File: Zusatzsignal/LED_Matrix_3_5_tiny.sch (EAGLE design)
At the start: 18 parts, among them IC3 ATTINY44SSU, Q1 IRLML5203, Q2 IRLML5203, Q3 IRLML5203, Q4 IRLML5203, Q5 IRLML5203, X1 TSW-106-02-S-S, X2 TSW-106-02-S-S-RA

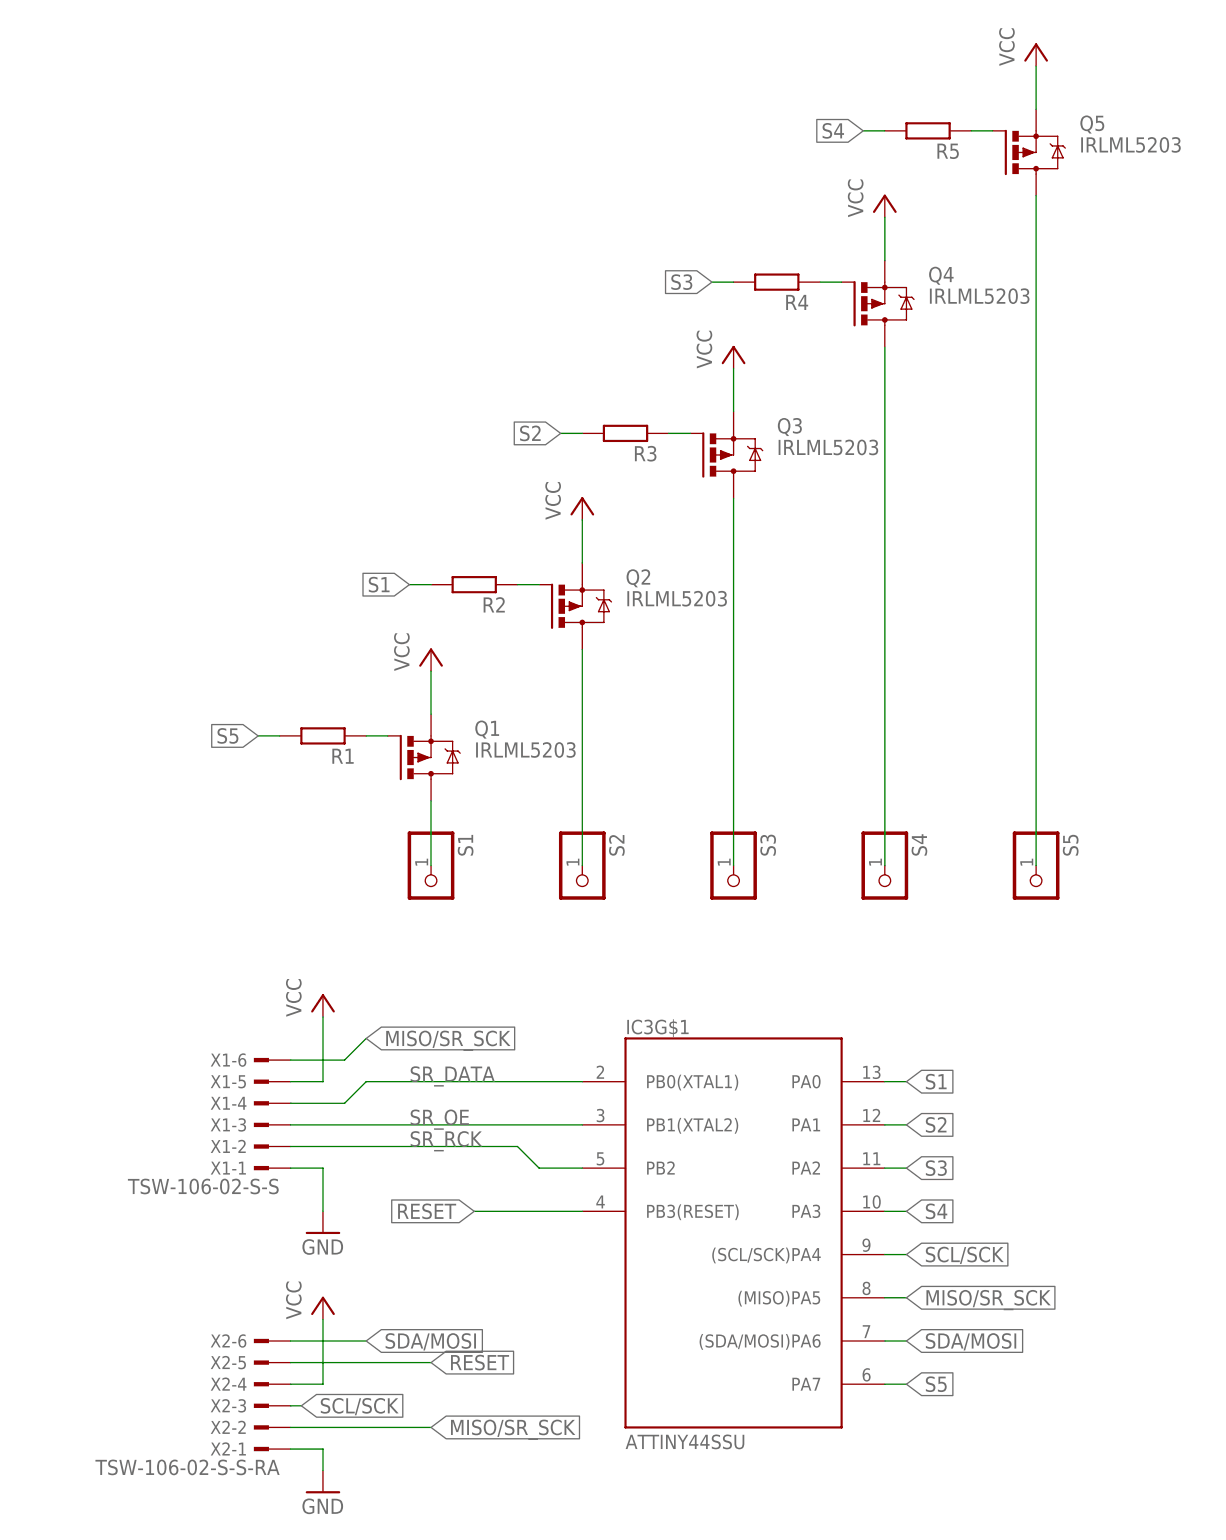
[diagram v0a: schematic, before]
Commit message: Verbesserung der Zusatzanzeigerplatine
- Änderung des Layouts der Rückseite
- Änderung der Durchführungen auf RM
- Beseitigung von DRC-Fehlern
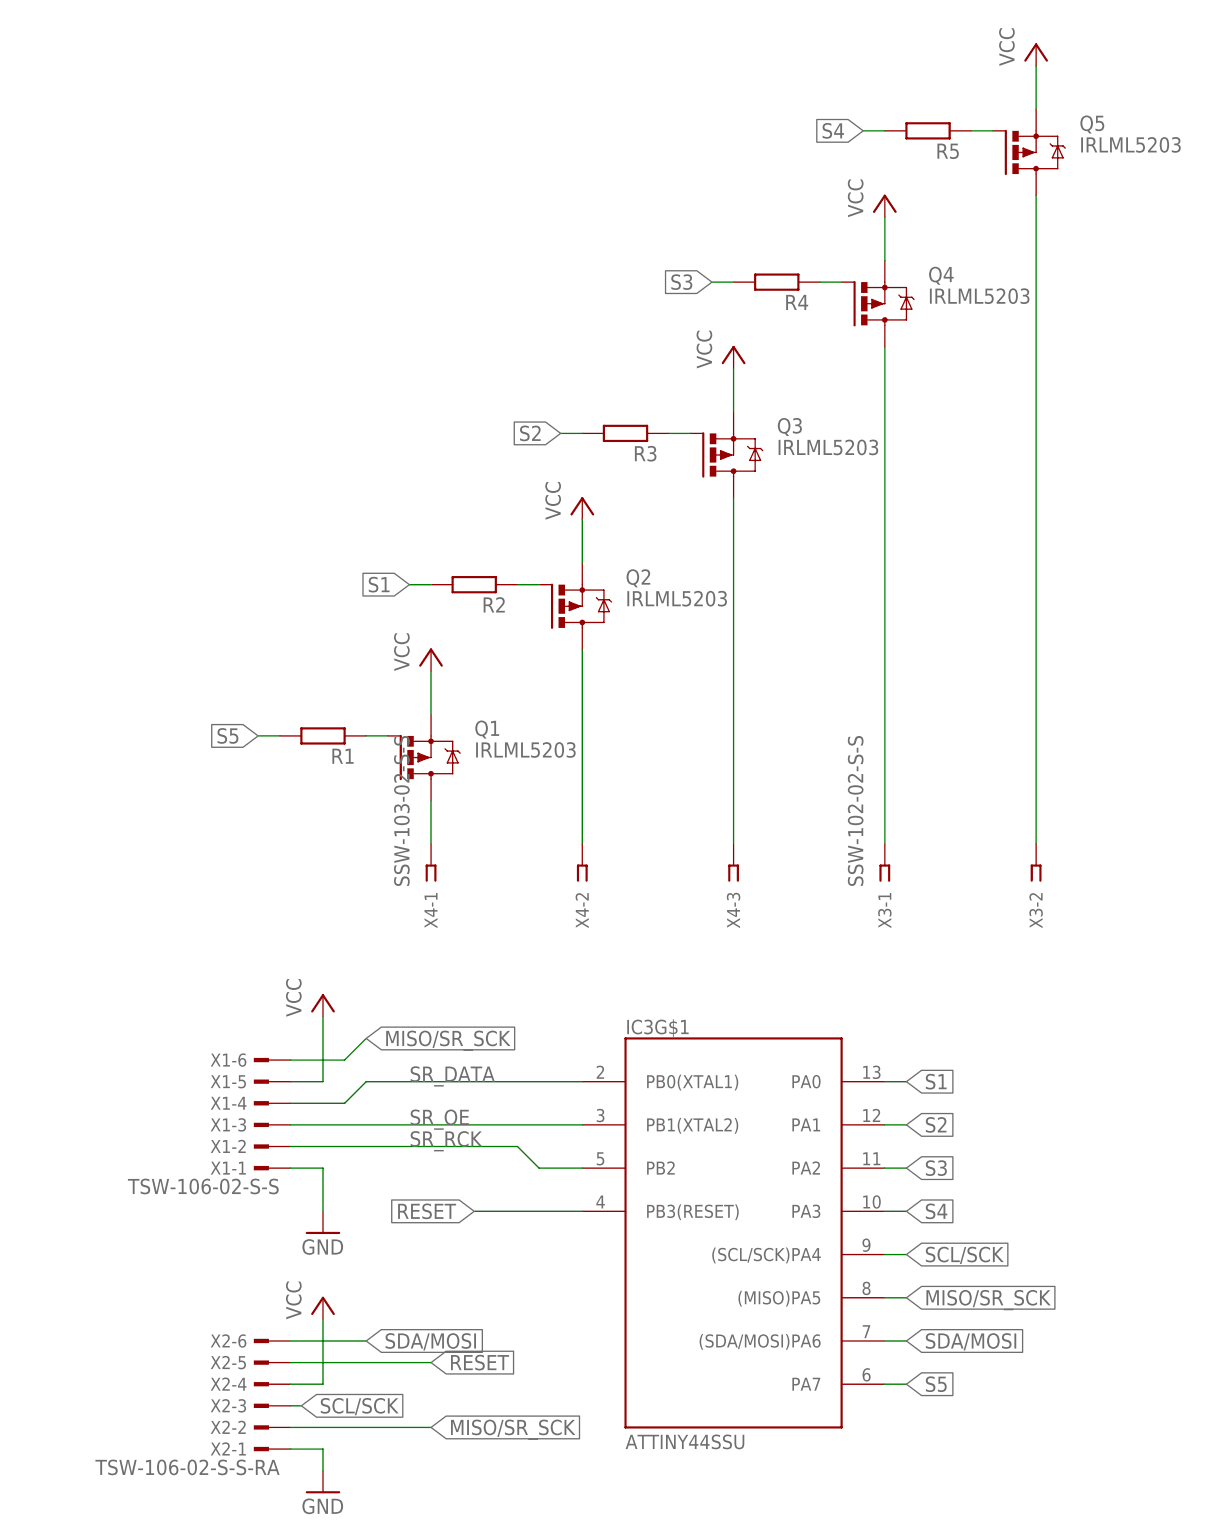
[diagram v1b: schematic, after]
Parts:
- removed S1, S2, S3, S4, S5: (no value), pinhead:PINHD-1X1
- added X3: SSW-102-02-S-S, con-samtec:SSW-102-02-S-S
- added X4: SSW-103-02-S-S, con-samtec:SSW-103-02-S-S
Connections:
- net N$19: now also X3-2.1; no longer S5.1
- net N$20: now also X3-1.1; no longer S4.1
- net N$21: now also X4-3.1; no longer S3.1
- net N$22: now also X4-2.1; no longer S2.1
- net N$23: now also X4-1.1; no longer S1.1
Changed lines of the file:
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@@
 </classes>
 <parts>
-<part name="S1" library="pinhead" deviceset="PINHD-1X1" device=""/>
-<part name="S2" library="pinhead" deviceset="PINHD-1X1" device=""/>
-<part name="S3" library="pinhead" deviceset="PINHD-1X1" device=""/>
-<part name="S4" library="pinhead" deviceset="PINHD-1X1" device=""/>
-<part name="S5" library="pinhead" deviceset="PINHD-1X1" device=""/>
 <part name="P+1" library="supply1" deviceset="VCC" device=""/>
 <part name="GND1" library="supply1" deviceset="GND" device=""/>
@@
 <part name="X1" library="con-samtec" library_urn="urn:adsk.eagle:library:184" deviceset="TSW-106-02-S-S" device=""/>
 <part name="X2" library="con-samtec" library_urn="urn:adsk.eagle:library:184" deviceset="TSW-106-02-S-S" device="-RA" value="TSW-106-02-S-S-RA"/>
+<part name="X3" library="con-samtec" library_urn="urn:adsk.eagle:library:184" deviceset="SSW-102-02-S-S" device=""/>
+<part name="X4" library="con-samtec" library_urn="urn:adsk.eagle:library:184" deviceset="SSW-103-02-S-S" device=""/>
 </parts>
 <sheets>
@@
 </plain>
 <instances>
-<instance part="S1" gate="G$1" x="33.02" y="114.3" rot="R270"/>
-<instance part="S2" gate="G$1" x="50.8" y="114.3" rot="R270"/>
-<instance part="S3" gate="G$1" x="68.58" y="114.3" rot="R270"/>
-<instance part="S4" gate="G$1" x="86.36" y="114.3" rot="R270"/>
-<instance part="S5" gate="G$1" x="104.14" y="114.3" rot="R270"/>
 <instance part="P+1" gate="VCC" x="20.32" y="66.04"/>
 <instance part="GND1" gate="1" x="20.32" y="43.18"/>
@@
 <instance part="X2" gate="-5" x="13.97" y="58.42" rot="R180"/>
 <instance part="X2" gate="-6" x="13.97" y="60.96" rot="R180"/>
+<instance part="X3" gate="-1" x="86.36" y="116.84" rot="R90"/>
+<instance part="X3" gate="-2" x="104.14" y="116.84" rot="R90"/>
+<instance part="X4" gate="-1" x="33.02" y="116.84" rot="R90"/>
+<instance part="X4" gate="-2" x="50.8" y="116.84" rot="R90"/>
+<instance part="X4" gate="-3" x="68.58" y="116.84" rot="R90"/>
 </instances>
 <busses>
@@
 <segment>
 <pinref part="Q5" gate="G$1" pin="D"/>
-<pinref part="S5" gate="G$1" pin="1"/>
-<wire x1="104.14" y1="116.84" x2="104.14" y2="195.58" width="0.1524" layer="91"/>
+<wire x1="104.14" y1="119.38" x2="104.14" y2="195.58" width="0.1524" layer="91"/>
+<pinref part="X3" gate="-2" pin="1"/>
 </segment>
 </net>
@@
 <segment>
 <pinref part="Q4" gate="G$1" pin="D"/>
-<pinref part="S4" gate="G$1" pin="1"/>
-<wire x1="86.36" y1="116.84" x2="86.36" y2="177.8" width="0.1524" layer="91"/>
+<wire x1="86.36" y1="119.38" x2="86.36" y2="177.8" width="0.1524" layer="91"/>
+<pinref part="X3" gate="-1" pin="1"/>
 </segment>
 </net>
@@
 <segment>
 <pinref part="Q3" gate="G$1" pin="D"/>
-<pinref part="S3" gate="G$1" pin="1"/>
-<wire x1="68.58" y1="116.84" x2="68.58" y2="160.02" width="0.1524" layer="91"/>
+<wire x1="68.58" y1="119.38" x2="68.58" y2="160.02" width="0.1524" layer="91"/>
+<pinref part="X4" gate="-3" pin="1"/>
 </segment>
 </net>
@@
 <segment>
 <pinref part="Q2" gate="G$1" pin="D"/>
-<pinref part="S2" gate="G$1" pin="1"/>
-<wire x1="50.8" y1="116.84" x2="50.8" y2="142.24" width="0.1524" layer="91"/>
+<wire x1="50.8" y1="119.38" x2="50.8" y2="142.24" width="0.1524" layer="91"/>
+<pinref part="X4" gate="-2" pin="1"/>
 </segment>
 </net>
@@
 <segment>
 <pinref part="Q1" gate="G$1" pin="D"/>
-<pinref part="S1" gate="G$1" pin="1"/>
-<wire x1="33.02" y1="116.84" x2="33.02" y2="124.46" width="0.1524" layer="91"/>
-</segment>
-</net>
+<wire x1="33.02" y1="119.38" x2="33.02" y2="124.46" width="0.1524" layer="91"/>
+<pinref part="X4" gate="-1" pin="1"/>
+</segment>
+</net>
